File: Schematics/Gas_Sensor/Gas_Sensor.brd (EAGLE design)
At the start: 46.7 x 45.7 mm, 7 parts, among them J1 RJ45

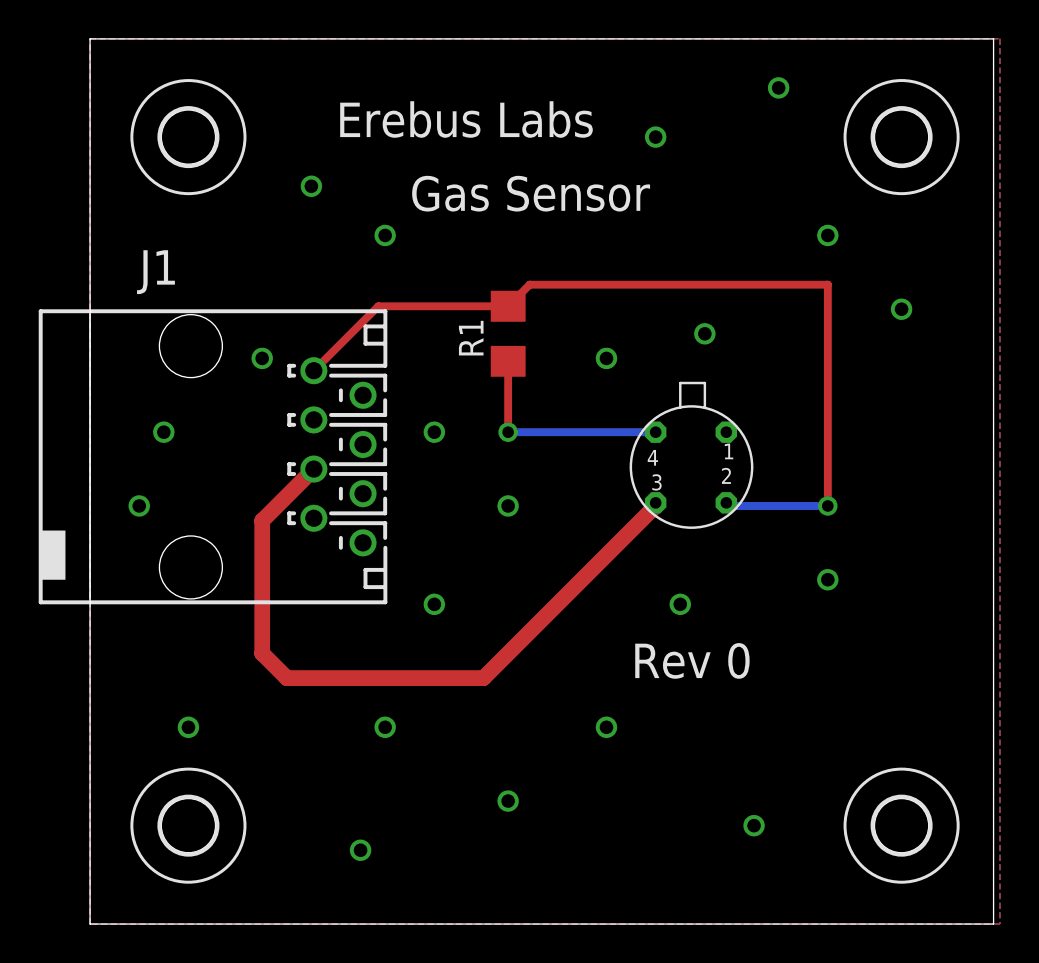
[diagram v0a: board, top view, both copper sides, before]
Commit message: Updated Sensor Module PCBs
Switched Ethernet I/O. Rerouted PCB
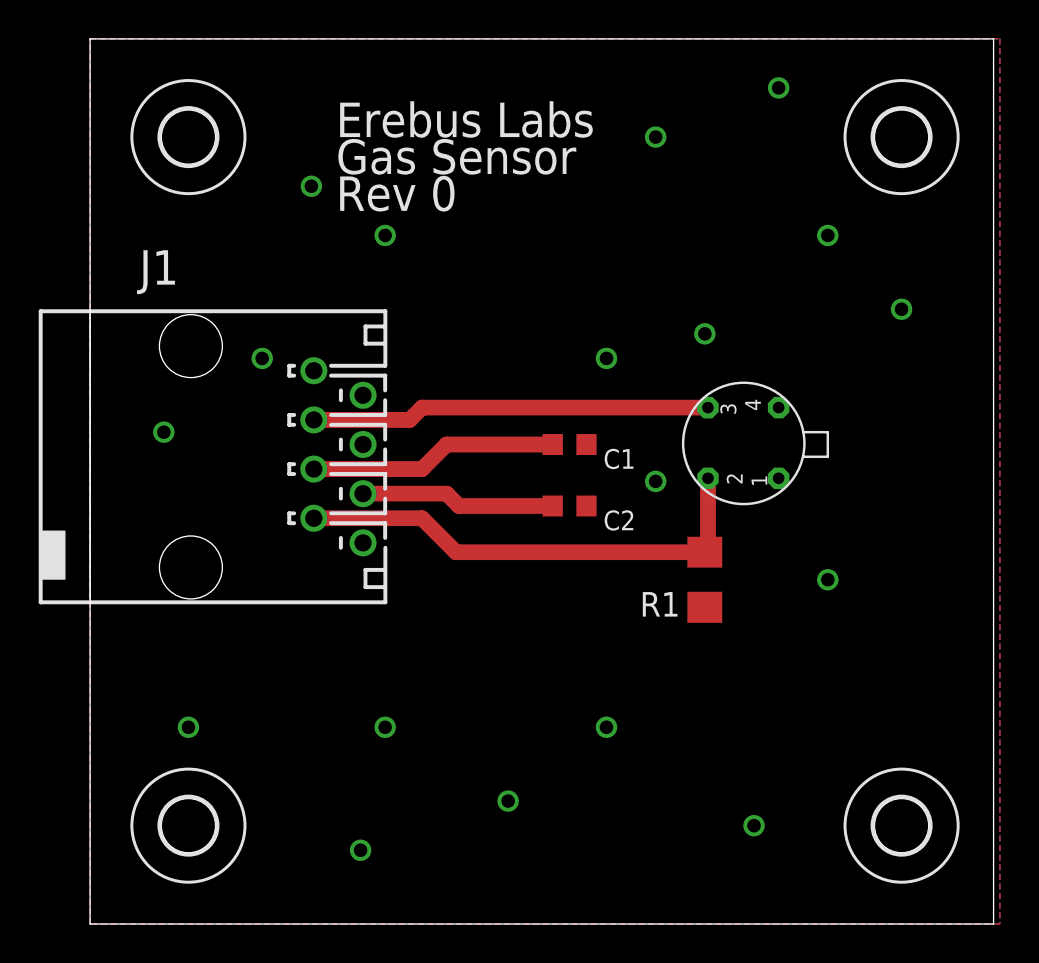
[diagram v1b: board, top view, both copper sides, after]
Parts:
- added C1, C2: (no value), rcl:C0603K
- moved R1 16.3 mm to (31.8, 52.1)
- moved U$1 6.48 mm to (35.6, 61.0), turned to 270 degrees
- renumbered H5 to H4
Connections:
- removed net +5V: J1.5, U$1.P$3
- new net N$24: C2.1, J1.6
- new net N$25: C1.1, J1.5
- new net N$26: J1.3, U$1.P$3
- net AGND: now also C1.2, C2.2, J1.1; no longer J1.3, J1.6, J1.7
- net N$2: now also J1.7; no longer J1.1
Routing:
- net +5V: track 35.3 -> 0.00 mm
- net N$26: track 0.00 -> 20.6 mm
- net N$2: track 45.1 -> 24.8 mm, vias 1 -> 0
- net N$25: track 0.00 -> 12.9 mm
- net AGND: track 11.4 -> 0.00 mm, vias 1 -> 18
- net N$24: track 0.00 -> 10.1 mm

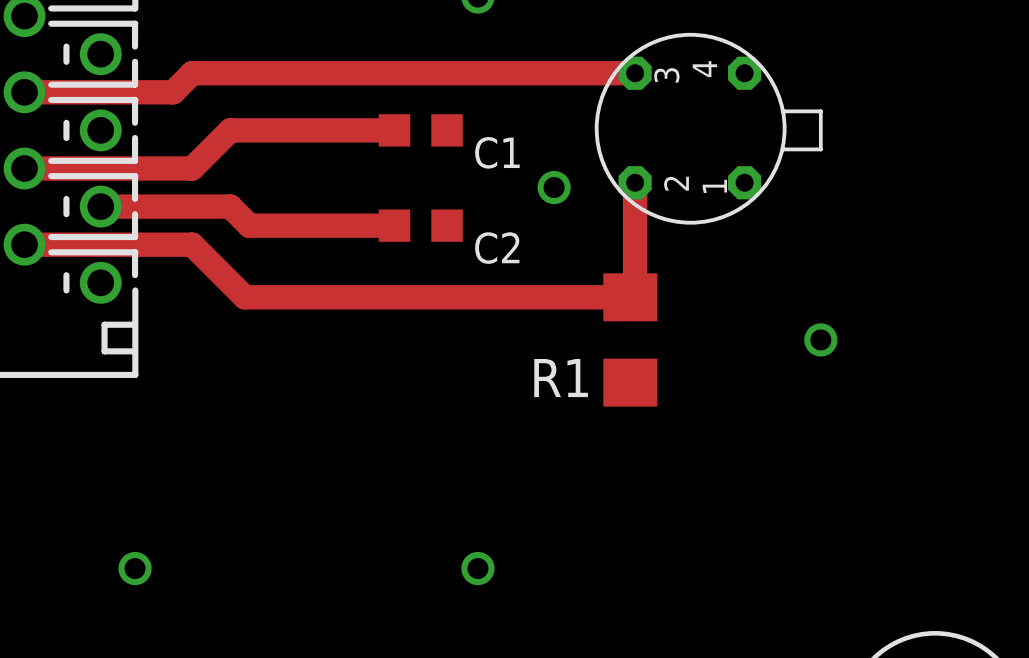
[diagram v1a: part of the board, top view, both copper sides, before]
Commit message: Began PCB Verify. Slight Modifications to Gas Sensor Module during verify.
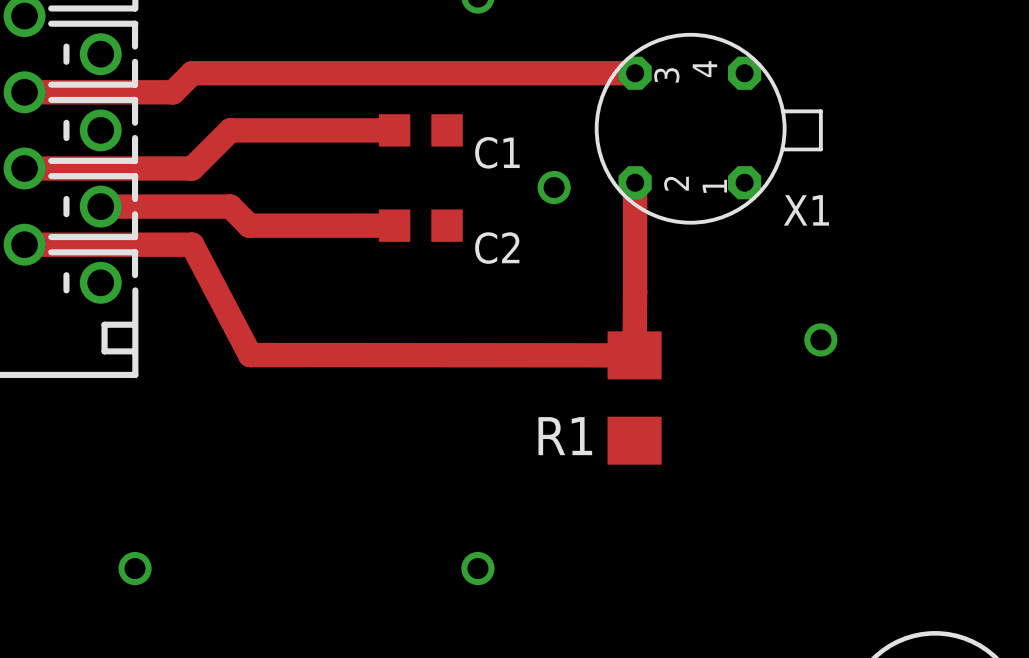
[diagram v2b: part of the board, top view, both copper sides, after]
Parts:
- moved R1 1.94 mm to (31.9, 50.1)
- renumbered U$1 to X1
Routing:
- net N$2: track 24.8 -> 28.3 mm
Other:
- board text added: "X1"
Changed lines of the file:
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@@
 <setting verticaltext="up"/>
 </settings>
-<grid distance="0.025" unitdist="inch" unit="inch" style="lines" multiple="1" display="no" altdistance="0.025" altunitdist="inch" altunit="inch"/>
+<grid distance="0" unitdist="inch" unit="inch" style="lines" multiple="1" display="yes" altdistance="0.025" altunitdist="inch" altunit="inch"/>
 <layers>
 <layer number="1" name="Top" color="4" fill="1" visible="yes" active="yes"/>
@@
 <text x="12.7" y="73.025" size="1.778" layer="21">Gas Sensor</text>
 <text x="12.7" y="71.12" size="1.778" layer="21">Rev 0</text>
+<text x="36.83" y="55.88" size="1.016" layer="25">X1</text>
 </plain>
 <attributes>
@@
 </autorouter>
 <elements>
-<element name="U$1" library="figaro" package="GAS_SENSOR" value="GAS_SENSOR" x="35.56" y="60.96" rot="R270"/>
-<element name="R1" library="rcl" package="R1206" value="30k" x="31.75" y="52.07" smashed="yes" rot="R90">
-<attribute name="NAME" x="30.48" y="51.435" size="1.27" layer="25" rot="R180"/>
-<attribute name="VALUE" x="30.48" y="49.53" size="1.27" layer="27" rot="R180"/>
+<element name="X1" library="figaro" package="GAS_SENSOR" value="GAS_SENSOR" x="35.56" y="60.96" rot="R270"/>
+<element name="R1" library="rcl" package="R1206" value="30k" x="31.891640625" y="50.13414375" smashed="yes" rot="R90">
+<attribute name="NAME" x="30.621640625" y="49.49914375" size="1.27" layer="25" rot="R180"/>
+<attribute name="VALUE" x="30.621640625" y="47.59414375" size="1.27" layer="27" rot="R180"/>
 </element>
 <element name="J1" library="con-amp" package="555167-1" value="RJ45" x="6.35" y="58.42" rot="R270"/>
@@
 <contactref element="C2" pad="2"/>
 <contactref element="J1" pad="4"/>
-<contactref element="U$1" pad="P$1"/>
-<contactref element="U$1" pad="P$2"/>
+<contactref element="X1" pad="P$1"/>
+<contactref element="X1" pad="P$2"/>
 <contactref element="J1" pad="8"/>
 <via x="13.97" y="38.1" extent="1-16" drill="0.7" diameter="0.4064"/>
@@
 <via x="15.24" y="69.85" extent="1-16" drill="0.7" diameter="0.4064"/>
 <via x="11.43" y="72.39" extent="1-16" drill="0.7" diameter="0.4064"/>
-<wire x1="15.24" y1="69.85" x2="11.43" y2="72.39" width="0" layer="19" extent="1-1"/>
 </signal>
 <signal name="N$2">
 <contactref element="R1" pad="2"/>
-<contactref element="U$1" pad="P$4"/>
+<contactref element="X1" pad="P$4"/>
 <contactref element="J1" pad="7"/>
 <wire x1="31.91" y1="57.31" x2="31.91" y2="53.652" width="0.8128" layer="1"/>
-<wire x1="31.91" y1="53.652" x2="31.75" y2="53.492" width="0.8128" layer="1"/>
-<wire x1="31.75" y1="53.492" x2="18.898" y2="53.492" width="0.8128" layer="1"/>
-<wire x1="18.898" y1="53.492" x2="17.145" y2="55.245" width="0.8128" layer="1"/>
+<wire x1="31.91" y1="53.652" x2="31.891640625" y2="51.55614375" width="0.8128" layer="1"/>
+<wire x1="31.891640625" y1="51.55614375" x2="19.077409375" y2="51.56563125" width="0.8128" layer="1"/>
+<wire x1="19.077409375" y1="51.56563125" x2="17.145" y2="55.245" width="0.8128" layer="1"/>
 <wire x1="17.145" y1="55.245" x2="11.557" y2="55.245" width="0.8128" layer="1"/>
 </signal>
@@
 <signal name="N$26">
 <contactref element="J1" pad="3"/>
-<contactref element="U$1" pad="P$3"/>
+<contactref element="X1" pad="P$3"/>
 <wire x1="11.557" y1="60.325" x2="16.51" y2="60.325" width="0.8128" layer="1"/>
 <wire x1="16.51" y1="60.325" x2="17.145" y2="60.96" width="0.8128" layer="1"/>
